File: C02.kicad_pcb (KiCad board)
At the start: 4 copper layers, 75.7 x 36.8 mm, 84 parts, among them J1 USB_B_Mini, J10 Conn_01x01, J11 ISP, J12 Conn_01x02, J2 Conn_01x10_Male, J3 Conn_01x06_Male, J4 Conn_01x08_Male, J5 Conn_01x08_Male, J6 Screw_Terminal_01x04, J7 Conn_01x01, J8 Conn_01x01, J9 Conn_01x01, U1 ATmega328PB-MU, U2 NME0505SC, U3 MIC5235-5.0, U4 LM393, U6 FT230XQ, U7 ISO7742, U8 ISO7740, Y1 16Mhz, 6pF

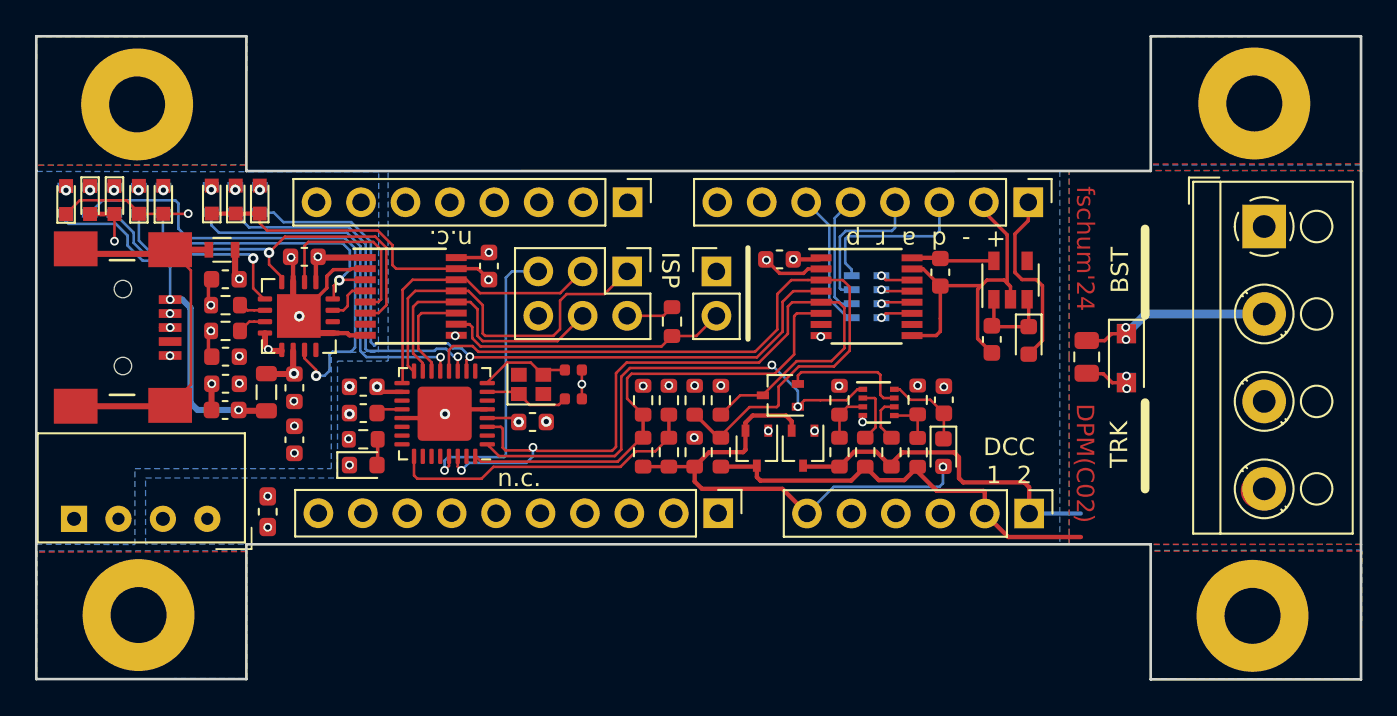
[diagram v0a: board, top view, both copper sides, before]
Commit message: mod: add JLCPCB part numbers
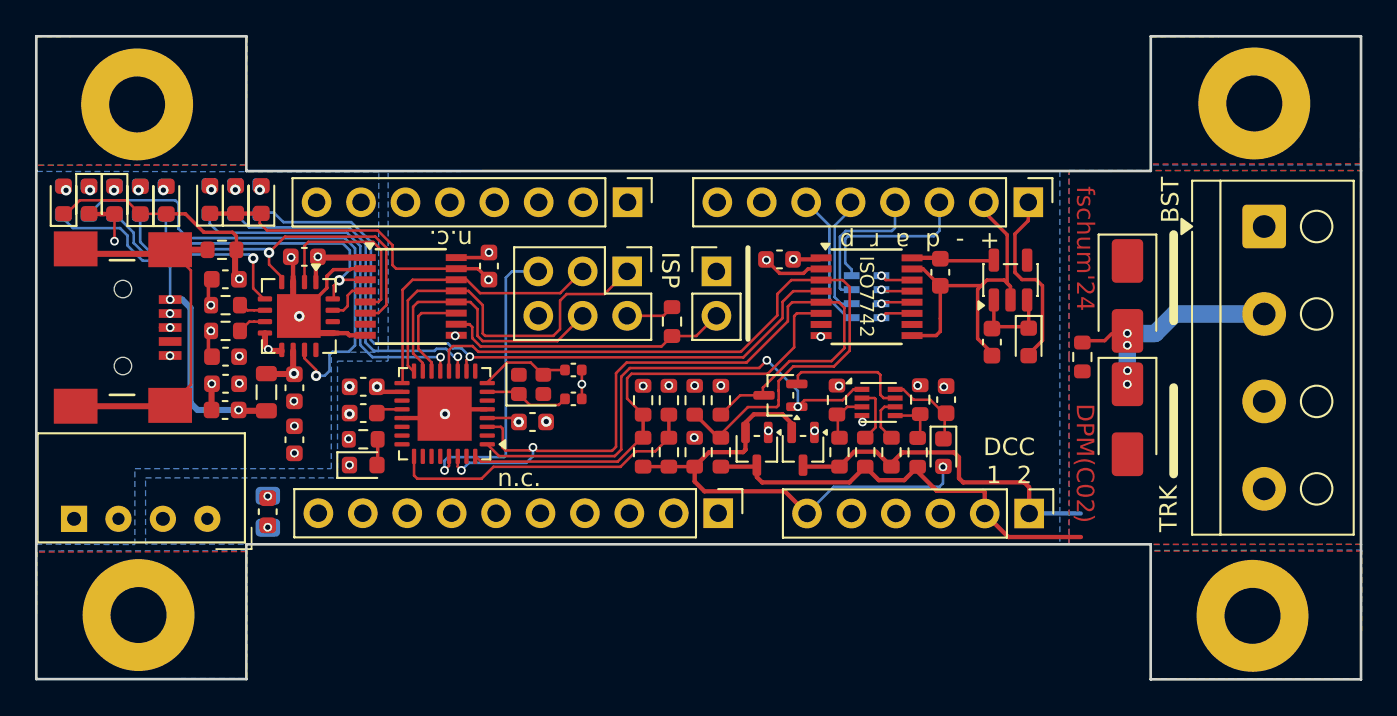
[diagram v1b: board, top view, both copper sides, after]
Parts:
- added R1: 220, Resistor_SMD:R_0805_2012Metric, B.Cu at (57.9, 50.1)
- C1: value 1u/35V -> 1u
- C6: value 4.7u/25V -> 10u/25V
- C8: footprint Capacitor_SMD:C_0603_1608Metric_Pad1.05x0.95mm_HandSolder -> Capacitor_SMD:C_0603_1608Metric
- D10: value SS34FA -> SSA33L; footprint Diode_SMD:D_SOD-123F -> Diode_SMD:D_SMA
- D11, D12, D13, D14, D15, D17, D18, D8: footprint LEDs:LED_0603 -> LED_SMD:LED_0603_1608Metric
- D19: value SS34FA -> SSA33L; footprint Diode_SMD:D_SOD-123F -> Diode_SMD:D_SMA; moved to F.Cu
- J2: footprint Pin_Headers:Pin_Header_Straight_1x10_Pitch2.54mm -> Connector_PinHeader_2.54mm:PinHeader_1x10_P2.54mm_Vertical
- J3: footprint Pin_Headers:Pin_Header_Straight_1x06_Pitch2.54mm -> Connector_PinHeader_2.54mm:PinHeader_1x06_P2.54mm_Vertical
- J4, J5: footprint Pin_Headers:Pin_Header_Straight_1x08_Pitch2.54mm -> Connector_PinHeader_2.54mm:PinHeader_1x08_P2.54mm_Vertical
- R15, R22, R23, R24: value 100k -> 4.7k; footprint Resistors_SMD:R_0603 -> Resistor_SMD:R_0603_1608Metric
- R21: footprint Resistor_SMD:R_0805_2012Metric -> Resistor_SMD:R_0603_1608Metric
- R25, R26, R27, R29, R30: footprint Resistors_SMD:R_0603 -> Resistor_SMD:R_0603_1608Metric
- R28: value 100k -> 4.7k
- U4: footprint Frank:DFN-8-1EP_NG_2x2mm_Pitch0.5mm -> Package_DFN_QFN:DFN-8_2x2mm_P0.5mm
- U7, U8: footprint Housings_SSOP:SSOP-16_3.9x4.9mm_Pitch0.635mm -> Package_SO:SSOP-16_3.9x4.9mm_P0.635mm
- moved D19 3.55 mm to (107.1, 37.8), turned to -90 degrees
- moved D10 3.49 mm to (107.1, 44.8)
- moved R21 0.25 mm to (104.5, 41.3)
- moved D17 0.18 mm to (52.1, 32.3)
- moved C2 0.16 mm to (99.3, 40.4)
- moved R7 0.15 mm to (95.2, 43.7)
- moved R33 0.14 mm to (90.5, 43.7)
- moved D8 0.14 mm to (46.3, 32.3)
- moved R29 0.14 mm to (52.1, 32.3)
- moved C1 0.13 mm to (96.7, 43.7)
- moved R15 0.11 mm to (46.2, 32.3)
- moved D13 0.10 mm to (54.6, 32.3)
- moved D15 0.09 mm to (57.6, 32.3)
- moved D2 0.08 mm to (101.4, 40.4)
- moved D18 0.08 mm to (50.7, 32.3)
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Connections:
- net ~CTS renamed ~{CTS}
- net ~RESET renamed ~{RESET}
- net ~RTS renamed ~{RTS}
- J1 pad 4: (no net) -> unconnected-(J1-ID-Pad4)
- J10 pad 1: Net-(J10-Pad1) -> unconnected-(J10-Pin_1-Pad1)
- J2 pad 1: (no net) -> unconnected-(J2-Pin_1-Pad1)
- J2 pad 10: (no net) -> unconnected-(J2-Pin_10-Pad10)
- J2 pad 2: (no net) -> unconnected-(J2-Pin_2-Pad2)
- J2 pad 3: (no net) -> unconnected-(J2-Pin_3-Pad3)
- J2 pad 4: (no net) -> unconnected-(J2-Pin_4-Pad4)
- J2 pad 5: (no net) -> unconnected-(J2-Pin_5-Pad5)
- J2 pad 6: (no net) -> unconnected-(J2-Pin_6-Pad6)
- J2 pad 7: (no net) -> unconnected-(J2-Pin_7-Pad7)
- J2 pad 8: (no net) -> unconnected-(J2-Pin_8-Pad8)
- J2 pad 9: (no net) -> unconnected-(J2-Pin_9-Pad9)
- J3 pad 3: (no net) -> unconnected-(J3-Pin_3-Pad3)
- J3 pad 4: (no net) -> unconnected-(J3-Pin_4-Pad4)
- J3 pad 5: (no net) -> unconnected-(J3-Pin_5-Pad5)
- J4 pad 7: (no net) -> unconnected-(J4-Pin_7-Pad7)
- J4 pad 8: (no net) -> unconnected-(J4-Pin_8-Pad8)
- J5 pad 1: (no net) -> unconnected-(J5-Pin_1-Pad1)
- J5 pad 2: (no net) -> unconnected-(J5-Pin_2-Pad2)
- J5 pad 3: (no net) -> unconnected-(J5-Pin_3-Pad3)
- J5 pad 4: (no net) -> unconnected-(J5-Pin_4-Pad4)
- J5 pad 5: (no net) -> unconnected-(J5-Pin_5-Pad5)
- J5 pad 6: (no net) -> unconnected-(J5-Pin_6-Pad6)
- J5 pad 7: (no net) -> unconnected-(J5-Pin_7-Pad7)
- J5 pad 8: (no net) -> unconnected-(J5-Pin_8-Pad8)
- J7 pad 1: Net-(J7-Pad1) -> unconnected-(J7-Pin_1-Pad1)
- J8 pad 1: Net-(J8-Pad1) -> unconnected-(J8-Pin_1-Pad1)
- J9 pad 1: Net-(J9-Pad1) -> unconnected-(J9-Pin_1-Pad1)
- U1 pad 19: (no net) -> unconnected-(U1-PE2-Pad19)
- U1 pad 2: (no net) -> unconnected-(U1-PD4-Pad2)
- U1 pad 22: (no net) -> unconnected-(U1-PE3-Pad22)
- U1 pad 23: (no net) -> unconnected-(U1-PC0-Pad23)
- U1 pad 24: (no net) -> unconnected-(U1-PC1-Pad24)
- U1 pad 26: (no net) -> unconnected-(U1-PC3-Pad26)
- U1 pad 27: (no net) -> unconnected-(U1-PC4-Pad27)
- U1 pad 28: (no net) -> unconnected-(U1-PC5-Pad28)
- U1 pad 31: (no net) -> unconnected-(U1-PD1-Pad31)
- U1 pad 6: (no net) -> unconnected-(U1-PE1-Pad6)
- U1 pad 9: (no net) -> unconnected-(U1-PD5-Pad9)
- U3 pad 4: (no net) -> unconnected-(U3-N.C.-Pad4)
- U6 pad 12: (no net) -> unconnected-(U6-CBUS0-Pad12)
- U6 pad 14: (no net) -> unconnected-(U6-CBUS3-Pad14)
- U7 pad 7: (no net) -> unconnected-(U7-EN1-Pad7)
- U8 pad 10: (no net) -> unconnected-(U8-EN2-Pad10)
- U8 pad 7: (no net) -> unconnected-(U8-NC-Pad7)
- Y1 pad 2: (no net) -> unconnected-(Y1-G-Pad2)
- Y1 pad 4: (no net) -> unconnected-(Y1-G-Pad2)_1
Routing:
- net GNDS: track 21.9 -> 25.8 mm, vias 9 -> 8
- net DCC-1: track 28.0 -> 25.1 mm, vias 2 -> 0
- net /Connectors/bstDCC-1: track 10.8 -> 12.8 mm, vias 2 -> 4
- net GNDD: track 28.2 -> 26.5 mm
- net ACK: track 42.4 -> 41.8 mm
- added copper zone on B.Cu, net unconnected-(J10-Pin_1-Pad1)
- added copper zone on F.Cu, net unconnected-(J10-Pin_1-Pad1)
- added copper zone on B.Cu, net unconnected-(J7-Pin_1-Pad1)
- added copper zone on F.Cu, net unconnected-(J7-Pin_1-Pad1)
- added copper zone on B.Cu, net unconnected-(J8-Pin_1-Pad1)
- added copper zone on F.Cu, net unconnected-(J8-Pin_1-Pad1)
- added copper zone on B.Cu, net unconnected-(J9-Pin_1-Pad1)
- added copper zone on F.Cu, net unconnected-(J9-Pin_1-Pad1)
- removed copper zone on B.Cu, net Net-(J10-Pad1)
- removed copper zone on F.Cu, net Net-(J10-Pad1)
- removed copper zone on B.Cu, net Net-(J7-Pad1)
- removed copper zone on F.Cu, net Net-(J7-Pad1)
- removed copper zone on B.Cu, net Net-(J8-Pad1)
- removed copper zone on F.Cu, net Net-(J8-Pad1)
- removed copper zone on B.Cu, net Net-(J9-Pad1)
- removed copper zone on F.Cu, net Net-(J9-Pad1)
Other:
- net class Default removed
- net class Power removed
- board text added: "ISO7742"
